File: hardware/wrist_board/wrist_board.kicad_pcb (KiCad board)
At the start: 4 copper layers, 60 x 42 mm, 56 parts, among them J1 S2B-PH-K-S_LF__SN_, J2 USB_C_Receptacle_USB2.0_14P, J3 Conn_01x02, J4 Conn_01x02, J5 Conn_01x02, J6 Conn_01x02, J7 Conn_01x02, J8 GPIOs, SW1 SW_SPST, U1 MCP73831T-2ACI_OT, U2 TLV75533PDBV, U3 MPU-6050, X1 ESP32-S3-WROOM-1-N16R8

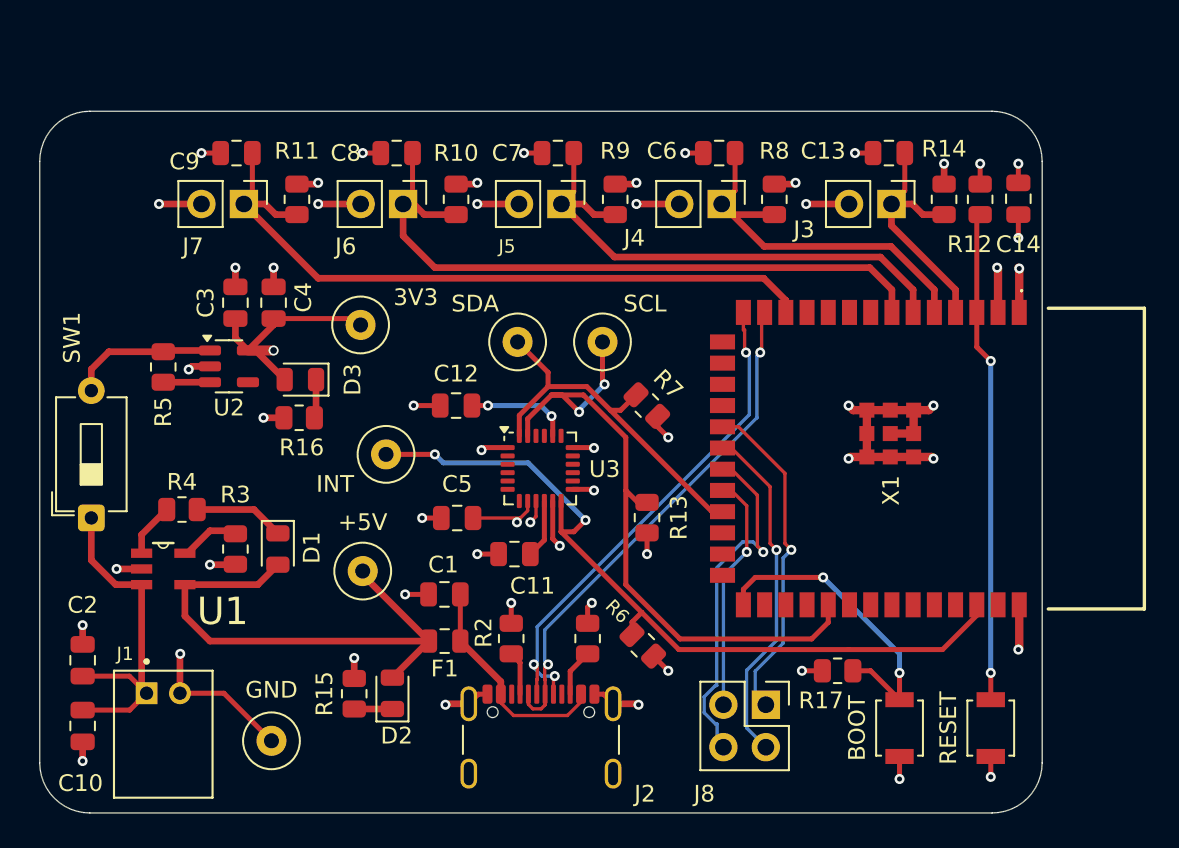
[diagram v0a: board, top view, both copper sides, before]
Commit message: Updates to wrist board for horizontal connections + mounting holes
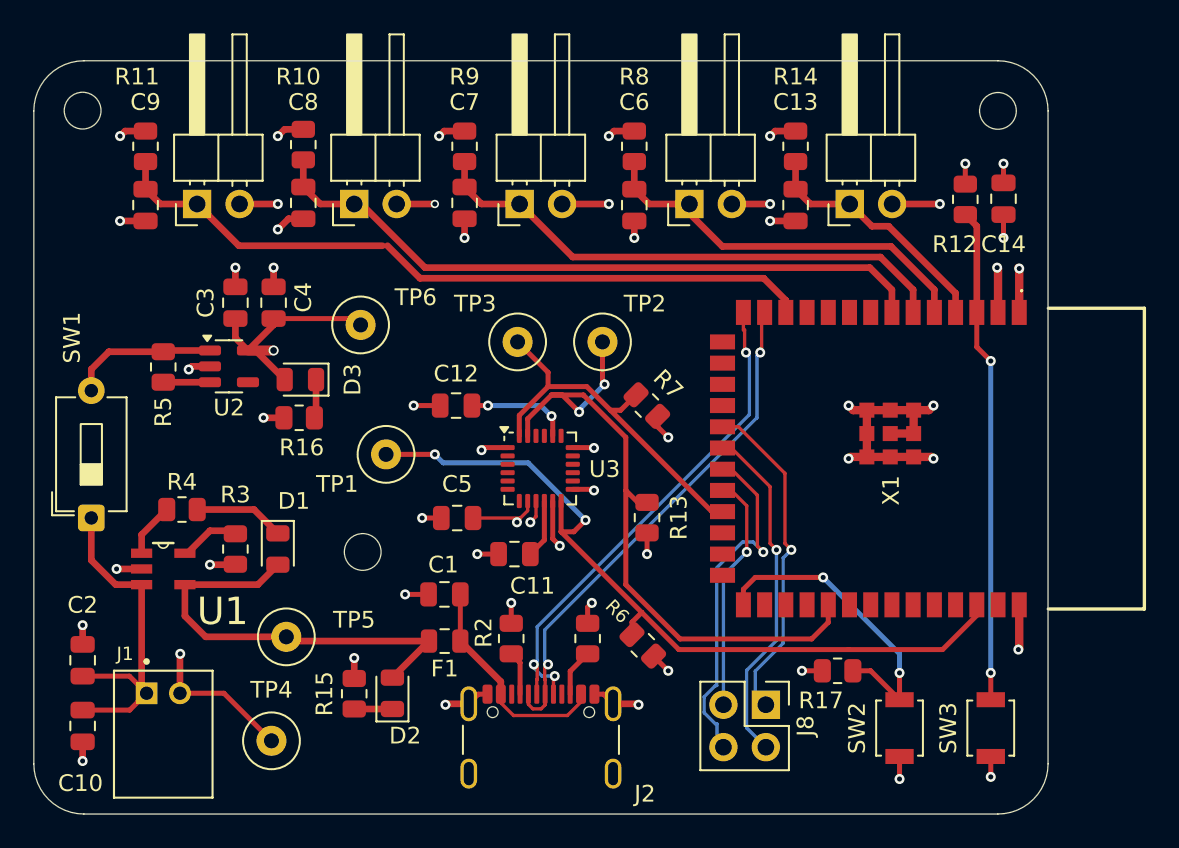
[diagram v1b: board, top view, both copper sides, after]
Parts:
- added REF**: MountingHole_2.2mm_M2, MountingHole:MountingHole_2.2mm_M2, F.Cu at (123.9, 85.9)
- added REF**: MountingHole_2.2mm_M2, MountingHole:MountingHole_2.2mm_M2, F.Cu at (85.9, 112.3)
- added REF**: MountingHole_2.2mm_M2, MountingHole:MountingHole_2.2mm_M2, F.Cu at (69.1, 85.9)
- J3, J4, J5, J6, J7: footprint Connector_PinHeader_2.54mm:PinHeader_1x02_P2.54mm_Vertical -> Connector_PinHeader_2.54mm:PinHeader_1x02_P2.54mm_Horizontal
- moved R10 9.71 mm to (82.3, 87.9)
- moved R11 9.60 mm to (72.9, 88.0)
- moved R9 9.56 mm to (91.9, 88.0)
- moved R14 9.44 mm to (111.8, 88.0)
- moved R8 8.96 mm to (102.1, 88.0)
- moved C13 6.40 mm to (111.8, 91.5), turned to -90 degrees
- moved C7 6.33 mm to (91.9, 91.4), turned to -90 degrees
- moved C8 6.33 mm to (82.3, 91.4), turned to -90 degrees
- moved C9 6.27 mm to (72.9, 91.5), turned to -90 degrees
- moved TP5 6.03 mm to (81.3, 117.3)
- moved C6 5.96 mm to (102.1, 91.5), turned to -90 degrees
- moved J6 2.93 mm to (85.3, 91.4), turned to 90 degrees
- moved J7 2.80 mm to (75.9, 91.4), turned to 90 degrees
- moved J3 2.50 mm to (115.0, 91.4), turned to 90 degrees
- moved J5 2.50 mm to (95.2, 91.4), turned to 90 degrees
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- renumbered BOOT to SW2, RESET to SW3, INT to TP1, SCL to TP2, SDA to TP3, GND to TP4, +5V to TP5, 3V3 to TP6
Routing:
- net +5V: track 32.1 -> 26.3 mm
- net GND: track 84.9 -> 86.8 mm
- net +3V3: track 37.0 -> 38.9 mm
- net /FS_5: track 42.2 -> 43.2 mm
- net /FS_3: track 31.4 -> 32.3 mm
- net /FS_2: track 23.0 -> 23.8 mm
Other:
- board size 60 x 42 mm -> 60.7 x 45.1 mm

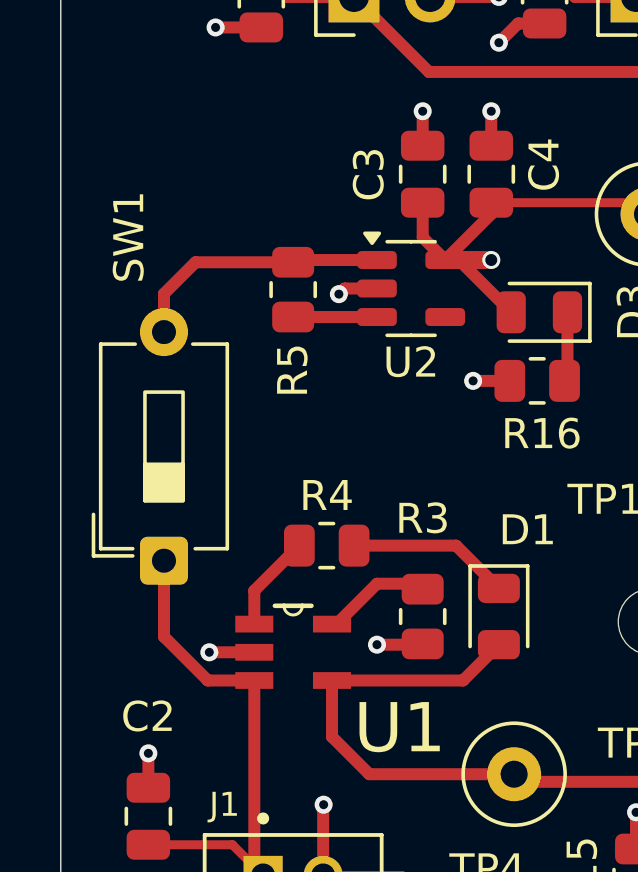
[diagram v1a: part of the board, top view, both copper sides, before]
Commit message: Added all JLC part numbers + generated production files
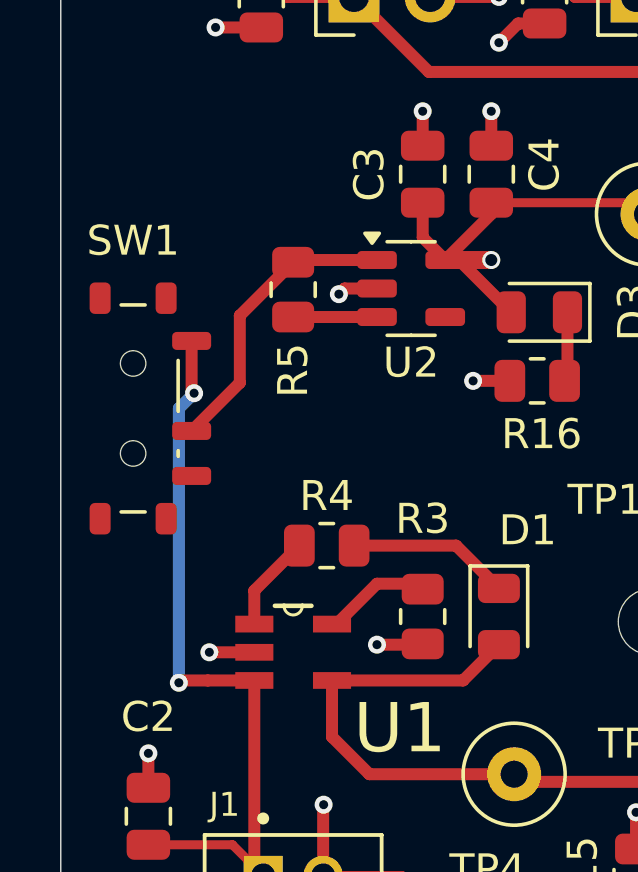
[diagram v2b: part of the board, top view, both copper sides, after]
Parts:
- SW1: footprint Button_Switch_THT:SW_DIP_SPSTx01_Slide_6.7x4.1mm_W7.62mm_P2.54mm_LowProfile -> Button_Switch_SMD:SW_SPDT_Shouhan_MSK12C02
- moved SW1 5.18 mm to (68.6, 105.2), turned to -90 degrees
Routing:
- net /<NO NET>: track 21.3 -> 29.3 mm, vias 0 -> 2
- net Net-(SW1-B): track 8.95 -> 9.96 mm

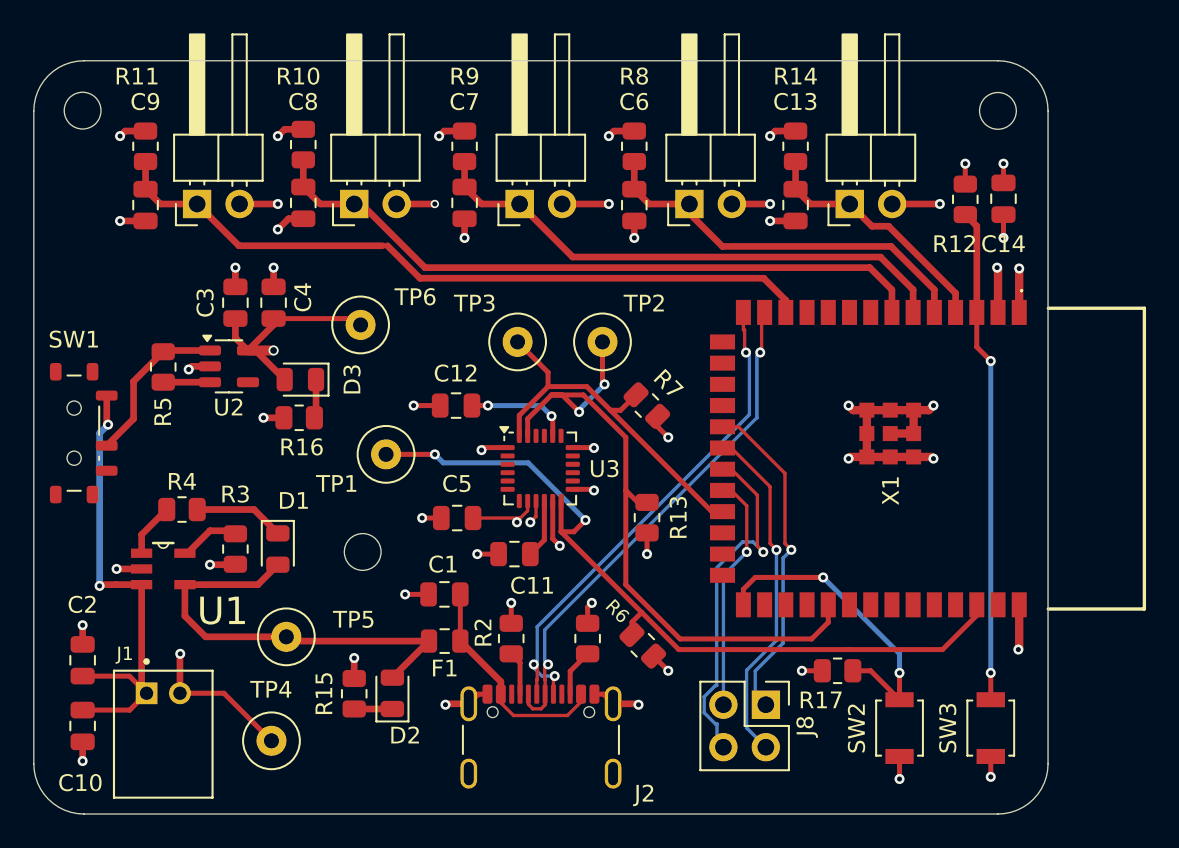
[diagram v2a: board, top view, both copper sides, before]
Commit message: Replaced old charging circuit, allows for input power derived from USB C or LIPO
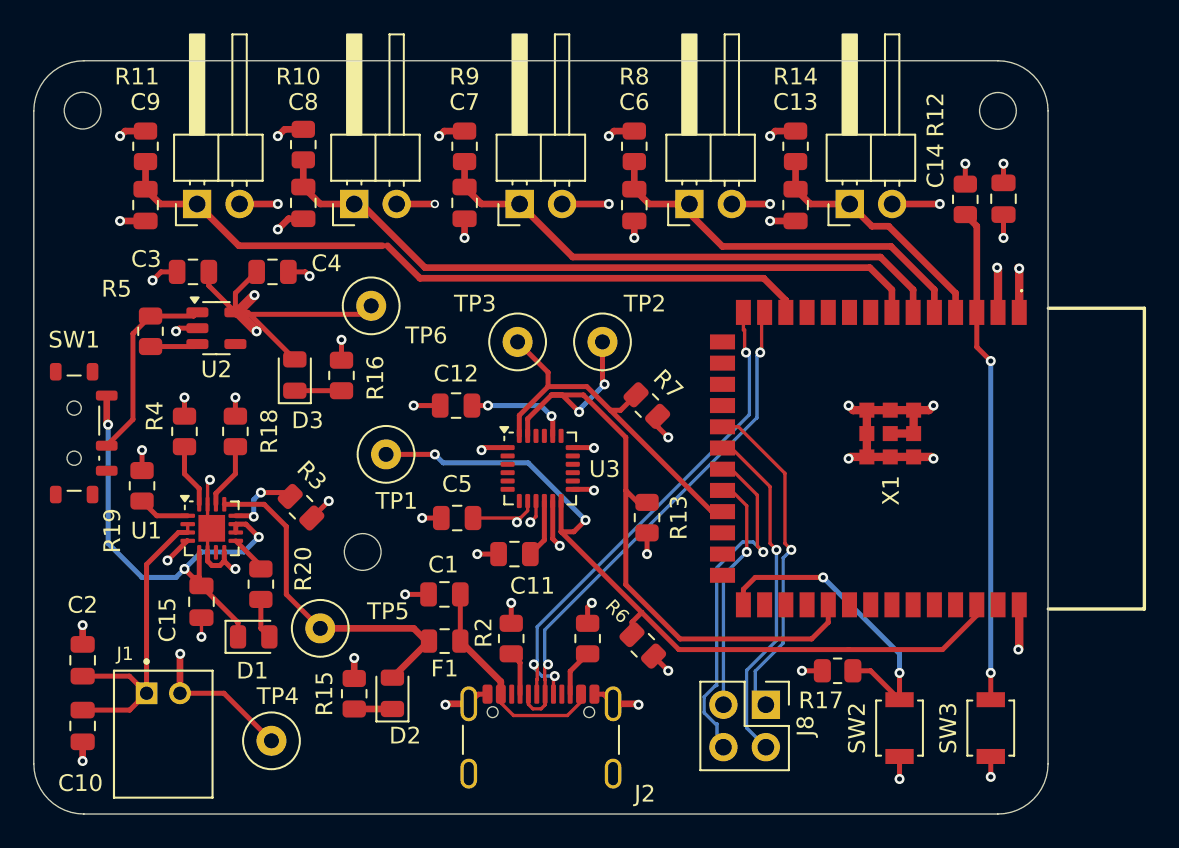
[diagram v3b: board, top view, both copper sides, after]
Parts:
- added C15: 10uF, Capacitor_SMD:C_0805_2012Metric, F.Cu at (76.2, 115.2)
- added R18: 46.4k, Resistor_SMD:R_0805_2012Metric, F.Cu at (78.2, 105.1)
- added R19: 10k, Resistor_SMD:R_0805_2012Metric, F.Cu at (72.6, 108.3)
- added R20: 1k, Resistor_SMD:R_0805_2012Metric, F.Cu at (79.8, 114.2)
- D1: value Charging LED -> CHG_LED
- R15, R16: value 10k -> 1k
- R3: value 10k -> 1.5k
- R4: value 470 -> 1.8k
- U1: value MCP73831T-2ACI_OT -> BQ24075RGT; footprint MCP73831T-2ACI_OT:SOT95P280X145-5N -> Package_DFN_QFN:VQFN-16-1EP_3x3mm_P0.5mm_EP1.6x1.6mm
- moved D1 5.45 mm to (79.3, 117.3), turned to 0 degrees
- moved R4 4.68 mm to (75.2, 105.1), turned to 90 degrees
- moved R3 4.66 mm to (82.2, 109.6), turned to -45 degrees
- moved U1 3.79 mm to (76.8, 110.9)
- moved R16 3.58 mm to (84.6, 101.7), turned to 90 degrees
- moved C3 3.14 mm to (75.7, 95.5), turned to 180 degrees
- moved U2 2.41 mm to (77.1, 98.9)
- moved R5 2.27 mm to (73.2, 99.1)
- moved TP5 2.09 mm to (83.3, 116.8)
- moved C4 1.85 mm to (80.5, 95.5), turned to 0 degrees
- moved TP6 1.31 mm to (86.4, 97.5)
- moved D3 0.43 mm to (81.8, 101.7), turned to 90 degrees
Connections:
- D1 pad 1: Net-(D1-K) -> /SYS
- D1 pad 2: +5V -> Net-(D1-A)
- R3 pad 1: Net-(U1-PROG) -> Net-(U1-ILIM)
- R4 pad 1: Net-(U1-STAT) -> Net-(U1-ISET)
- R4 pad 2: Net-(D1-K) -> GND
- SW1 pad 1: /<NO NET> -> /SYS
- U1 pad 1: Net-(U1-STAT) -> Net-(U1-TS)
- U1 pad 2: GND -> /<NO NET>
- U1 pad 4: +5V -> GND
- U1 pad 5: Net-(U1-PROG) -> /SYS
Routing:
- net /SYS: track 0.00 -> 29.1 mm, vias 0 -> 3
- net GND: track 86.8 -> 100.1 mm, vias 41 -> 47
- net /<NO NET>: track 29.3 -> 20.4 mm, vias 2 -> 0
- net +3V3: track 38.9 -> 46.7 mm, vias 15 -> 16
- net Net-(D1-K): track 5.42 -> 0.00 mm
- net +5V: track 26.3 -> 21.1 mm
- net Net-(U1-ILIM): track 0.00 -> 4.57 mm, vias 0 -> 2
- net Net-(U1-TMR): track 0.00 -> 3.93 mm
- net Net-(U1-ISET): track 0.00 -> 3.81 mm
- net Net-(U1-PROG): track 3.65 -> 0.00 mm
- net Net-(U1-STAT): track 3.24 -> 0.00 mm
- net Net-(U1-TS): track 0.00 -> 3.10 mm
- net Net-(D1-A): track 0.00 -> 2.45 mm
- net Net-(U1-~{CHG}): track 0.00 -> 2.30 mm
- net Net-(SW1-B): track 9.96 -> 11.7 mm

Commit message: Replaced dupont headers with screw terminal
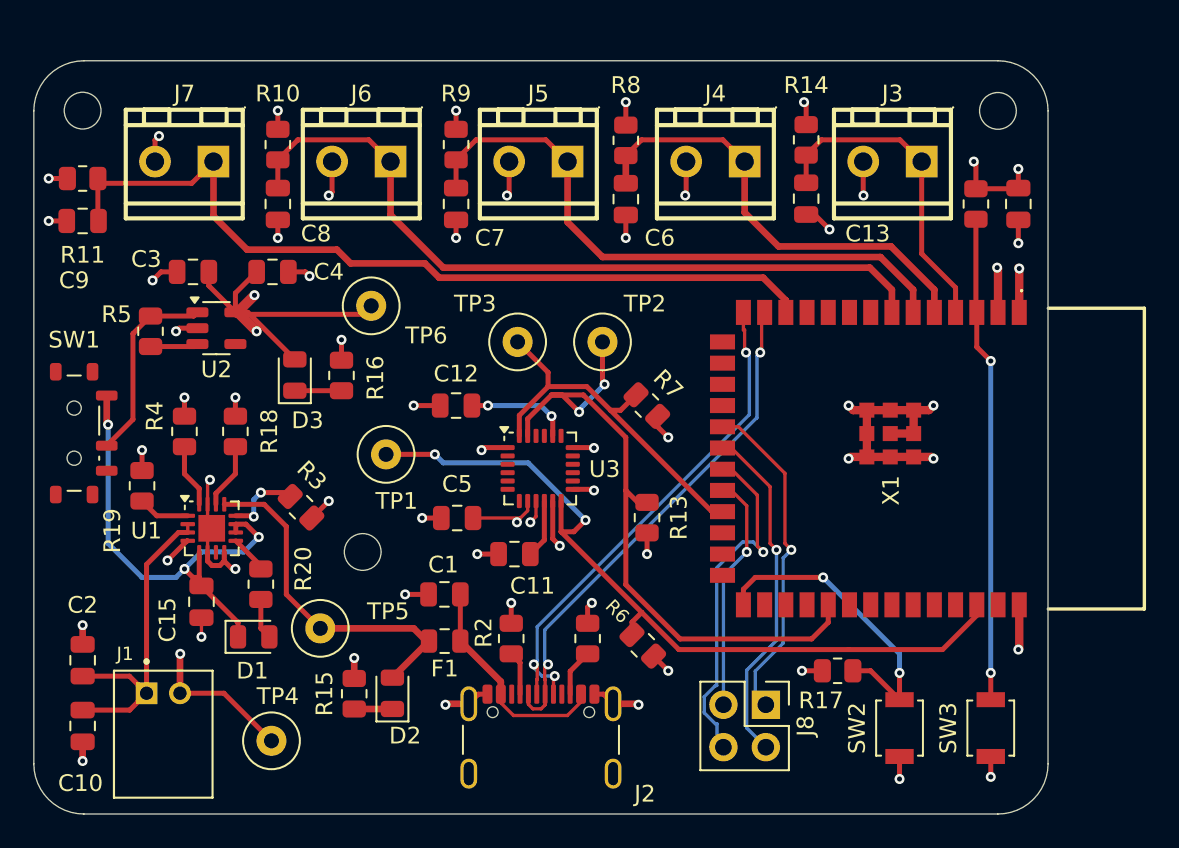
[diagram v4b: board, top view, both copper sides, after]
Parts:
- J3, J4, J5, J6, J7: footprint Connector_PinHeader_2.54mm:PinHeader_1x02_P2.54mm_Horizontal -> easyeda2kicad:CONN-TH_DG350-3.5-02P-14-00A-H
- moved R11 4.23 mm to (69.1, 89.9), turned to 180 degrees
- moved C9 3.88 mm to (69.1, 92.5), turned to 180 degrees
- moved J3 3.61 mm to (117.6, 88.9), turned to 180 degrees
- moved J4 2.98 mm to (107.0, 88.9), turned to 180 degrees
- moved J5 2.78 mm to (96.4, 88.9), turned to 180 degrees
- moved J7 2.65 mm to (75.2, 88.9), turned to 180 degrees
- moved J6 2.58 mm to (85.8, 88.9), turned to 180 degrees
- moved C8 1.53 mm to (80.8, 91.4)
- moved R10 1.52 mm to (80.8, 87.9)
- moved C14 0.94 mm to (125.1, 91.4)
- moved C13 0.74 mm to (112.4, 91.1)
- moved R14 0.74 mm to (112.4, 87.6)
- moved R12 0.69 mm to (122.6, 91.4)
- moved C6 0.62 mm to (101.6, 91.1)
- moved R8 0.62 mm to (101.6, 87.6)
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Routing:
- net /FS_5: track 43.2 -> 50.5 mm
- net /FS_4: track 40.8 -> 45.9 mm
- net /FS_3: track 32.3 -> 36.7 mm
- net /FS_1: track 15.0 -> 19.4 mm
- net GND: track 100.1 -> 96.2 mm
- net /FS_2: track 23.8 -> 27.4 mm
- net +3V3: track 46.7 -> 47.6 mm
- net /EN: track 29.9 -> 29.1 mm
